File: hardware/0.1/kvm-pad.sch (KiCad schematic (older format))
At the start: 10 parts, among them J1 USB_C_Receptacle_USB2.0, J2 USB_C_Receptacle_USB2.0, U1 USBLC6-2SC6, U2 USBLC6-2SC6

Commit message: add mcu + 2x4 switches + icsp
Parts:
- added C1, C6: 1u, symbol Device:C
- added C2, C3: 100n, symbol Device:C
- added C4, C5: 22p, symbol Device:C
- added D1, D2, D3, D4, D5, D6, D7, D8: D, Diode_SMD:D_SOD-123, symbol Device:D_Small
- added J3: AVR-ISP-6, josh-connectors:AVR_PROG_2.54_SMT, symbol Connector:AVR-ISP-6
- added K1, K2, K3, K4, K5, K6, K7, K8: KEYSW, josh-keyboard:MX_KEYSWITCH, symbol Switch:SW_Push
- added R1, R2: 22R, symbol Device:R
- added R3: 10K, symbol Device:R
- added U2: ATMEGA32U4, symbol josh-ic:ATMEGA32U4
- added Y1: 16MHz, symbol Device:Crystal_GND24_Small
- renumbered U2 to U3
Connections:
- net GND: now also C1.2, C2.2, C3.2, C4.2, C5.2, C6.2, J3.6 (GND), R3.2, U2.15 (GND), U2.23 (GND), U2.35 (GND), U2.43 (GND), U2.5 (UGnd), Y1.2, Y1.4
- new net: C4.1, U2.16 (XTAL1), Y1.1
- new net: C5.1, U2.17 (XTAL2), Y1.3
- new net: R2.1, U2.3 (D-)
- new net: R3.1, U2.33 (PE2/~HWB)
- new net: R1.1, U2.4 (D+)
- new net: C6.1, U2.6 (UCap)
- new net: D1.2 (A), K1.2
- new net: D5.2 (A), K5.2
- new net: D2.2 (A), K2.2
- new net: D6.2 (A), K6.2
- new net: D4.2 (A), K4.2
- new net: D8.2 (A), K8.2
- new net: D7.2 (A), K7.2
- new net: D3.2 (A), K3.2
- new net +5V: C1.1, C2.1, C3.1, J3.2 (VCC), U2.14 (VCC), U2.2 (UVcc), U2.24 (AVCC), U2.34 (VCC), U2.42 (AREF), U2.44 (AVCC), U2.7 (VBus)
- new net MCU_D+: R1.2
- new net MCU_D-: R2.2
- new net MISO: J3.1 (MISO), U2.11 (PB3/MISO)
- new net MOSI: J3.4 (MOSI), U2.10 (PB2/MOSI)
- new net SCK: J3.3 (SCK), U2.9 (PB1/SCK)
- new net SWITCH: U2.27 (PD7)
- new net col1: K1.1, K5.1, U2.18 (PD0)
- new net col2: K2.1, K6.1, U2.19 (PD1)
- new net col3: K3.1, K7.1, U2.20 (PD2)
- new net col4: K4.1, K8.1, U2.21 (PD3)
- new net nRST: J3.5 (~RST), U2.13 (~RESET)
- new net row1: D1.1 (K), D2.1 (K), D3.1 (K), D4.1 (K), U2.41 (PF0)
- new net row2: D5.1 (K), D6.1 (K), D7.1 (K), D8.1 (K), U2.40 (PF1)
- no-connect marks 7 -> 19
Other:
- note added: "ICSP"
- note added: "Microcontroller"
- note added: "Switch Array"

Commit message: Update jkl & footprints
USBA / Kailh Choc / ATMEGA32U4-AU
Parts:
- K1, K2, K3, K4, K5, K6, K7, K8: footprint josh-keyboard:MX_KEYSWITCH -> josh-keyboard:Choc_Hotswap
- U2: footprint (none) -> josh-dfn-qfn:ATMEGA32U4-AU
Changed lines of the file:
@@
 F 0 "U2" H 5825 3962 60  0000 C CNN
 F 1 "ATMEGA32U4" H 5825 3856 60  0000 C CNN
-F 2 "" H 6025 2625 60  0000 C CNN
+F 2 "josh-dfn-qfn:ATMEGA32U4-AU" H 6025 2625 60  0001 C CNN
 F 3 "" H 6025 2625 60  0000 C CNN
 	1    6025 2625
@@
 F 0 "K1" H 7875 1425 60  0000 C CNN
 F 1 "KEYSW" H 7875 1150 60  0001 C CNN
-F 2 "josh-keyboard:MX_KEYSWITCH" H 7875 1250 60  0001 C CNN
+F 2 "josh-keyboard:Choc_Hotswap" H 7875 1250 60  0001 C CNN
 F 3 "" H 7875 1250 60  0000 C CNN
 F 4 "" H 7875 1250 50  0001 C CNN "Notes"
@@
 F 0 "K5" H 7875 2025 60  0000 C CNN
 F 1 "KEYSW" H 7875 1750 60  0001 C CNN
-F 2 "josh-keyboard:MX_KEYSWITCH" H 7875 1850 60  0001 C CNN
+F 2 "josh-keyboard:Choc_Hotswap" H 7875 1850 60  0001 C CNN
 F 3 "" H 7875 1850 60  0000 C CNN
 F 4 "" H 7875 1850 50  0001 C CNN "Notes"
@@
 F 0 "K2" H 8775 1425 60  0000 C CNN
 F 1 "KEYSW" H 8775 1150 60  0001 C CNN
-F 2 "josh-keyboard:MX_KEYSWITCH" H 8775 1250 60  0001 C CNN
+F 2 "josh-keyboard:Choc_Hotswap" H 8775 1250 60  0001 C CNN
 F 3 "" H 8775 1250 60  0000 C CNN
 F 4 "" H 8775 1250 50  0001 C CNN "Notes"
@@
 F 0 "K6" H 8775 2025 60  0000 C CNN
 F 1 "KEYSW" H 8775 1750 60  0001 C CNN
-F 2 "josh-keyboard:MX_KEYSWITCH" H 8775 1850 60  0001 C CNN
+F 2 "josh-keyboard:Choc_Hotswap" H 8775 1850 60  0001 C CNN
 F 3 "" H 8775 1850 60  0000 C CNN
 F 4 "" H 8775 1850 50  0001 C CNN "Notes"
@@
 F 0 "K4" H 10575 1425 60  0000 C CNN
 F 1 "KEYSW" H 10575 1150 60  0001 C CNN
-F 2 "josh-keyboard:MX_KEYSWITCH" H 10575 1250 60  0001 C CNN
+F 2 "josh-keyboard:Choc_Hotswap" H 10575 1250 60  0001 C CNN
 F 3 "" H 10575 1250 60  0000 C CNN
 F 4 "" H 10575 1250 50  0001 C CNN "Notes"
@@
 F 0 "K8" H 10575 2025 60  0000 C CNN
 F 1 "KEYSW" H 10575 1750 60  0001 C CNN
-F 2 "josh-keyboard:MX_KEYSWITCH" H 10575 1850 60  0001 C CNN
+F 2 "josh-keyboard:Choc_Hotswap" H 10575 1850 60  0001 C CNN
 F 3 "" H 10575 1850 60  0000 C CNN
 F 4 "" H 10575 1850 50  0001 C CNN "Notes"
@@
 F 0 "K7" H 9675 2025 60  0000 C CNN
 F 1 "KEYSW" H 9675 1750 60  0001 C CNN
-F 2 "josh-keyboard:MX_KEYSWITCH" H 9675 1850 60  0001 C CNN
+F 2 "josh-keyboard:Choc_Hotswap" H 9675 1850 60  0001 C CNN
 F 3 "" H 9675 1850 60  0000 C CNN
 F 4 "" H 9675 1850 50  0001 C CNN "Notes"
@@
 F 0 "K3" H 9700 1425 60  0000 C CNN
 F 1 "KEYSW" H 9700 1150 60  0001 C CNN
-F 2 "josh-keyboard:MX_KEYSWITCH" H 9700 1250 60  0001 C CNN
+F 2 "josh-keyboard:Choc_Hotswap" H 9700 1250 60  0001 C CNN
 F 3 "" H 9700 1250 60  0000 C CNN
 F 4 "" H 9700 1250 50  0001 C CNN "Notes"

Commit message: Add missing footprints
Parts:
- C1, C2, C3, C4, C5, C6: footprint (none) -> Capacitor_SMD:C_0603_1608Metric
- R1, R2, R3: footprint (none) -> Resistor_SMD:R_0603_1608Metric
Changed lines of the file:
@@
 F 0 "C3" V 4625 1250 50  0000 C CNN
 F 1 "100n" V 4725 1250 50  0000 C CNN
-F 2 "" H 4713 1250 50  0001 C CNN
+F 2 "Capacitor_SMD:C_0603_1608Metric" H 4713 1250 50  0001 C CNN
 F 3 "~" H 4675 1400 50  0001 C CNN
 	1    4675 1400
@@
 F 0 "C2" V 4625 1025 50  0000 C CNN
 F 1 "100n" V 4725 1025 50  0000 C CNN
-F 2 "" H 4713 1025 50  0001 C CNN
+F 2 "Capacitor_SMD:C_0603_1608Metric" H 4713 1025 50  0001 C CNN
 F 3 "~" H 4675 1175 50  0001 C CNN
 	1    4675 1175
@@
 F 0 "C1" V 4625 800 50  0000 C CNN
 F 1 "1u" V 4725 800 50  0000 C CNN
-F 2 "" H 4713 800 50  0001 C CNN
+F 2 "Capacitor_SMD:C_0603_1608Metric" H 4713 800 50  0001 C CNN
 F 3 "~" H 4675 950 50  0001 C CNN
 	1    4675 950
@@
 F 0 "C4" V 4325 2775 50  0000 C CNN
 F 1 "22p" V 4425 2775 50  0000 C CNN
-F 2 "" H 4413 2775 50  0001 C CNN
+F 2 "Capacitor_SMD:C_0603_1608Metric" H 4413 2775 50  0001 C CNN
 F 3 "~" H 4375 2925 50  0001 C CNN
 	1    4375 2925
@@
 F 0 "C5" V 4325 2975 50  0000 C CNN
 F 1 "22p" V 4425 2975 50  0000 C CNN
-F 2 "" H 4413 2975 50  0001 C CNN
+F 2 "Capacitor_SMD:C_0603_1608Metric" H 4413 2975 50  0001 C CNN
 F 3 "~" H 4375 3125 50  0001 C CNN
 	1    4375 3125
@@
 F 0 "R3" H 4695 3721 50  0000 L CNN
 F 1 "10K" H 4695 3630 50  0000 L CNN
-F 2 "" V 4555 3675 50  0001 C CNN
+F 2 "Resistor_SMD:R_0603_1608Metric" V 4555 3675 50  0001 C CNN
 F 3 "~" H 4625 3675 50  0001 C CNN
 	1    4625 3675
@@
 F 0 "C6" H 4440 3721 50  0000 L CNN
 F 1 "1u" H 4440 3630 50  0000 L CNN
-F 2 "" H 4363 3525 50  0001 C CNN
+F 2 "Capacitor_SMD:C_0603_1608Metric" H 4363 3525 50  0001 C CNN
 F 3 "~" H 4325 3675 50  0001 C CNN
 	1    4325 3675
@@
 F 0 "R1" V 4725 2375 50  0000 C CNN
 F 1 "22R" V 4825 2375 50  0000 C CNN
-F 2 "" V 4755 2375 50  0001 C CNN
+F 2 "Resistor_SMD:R_0603_1608Metric" V 4755 2375 50  0001 C CNN
 F 3 "~" H 4825 2375 50  0001 C CNN
 	1    4825 2375
@@
 F 0 "R2" V 4925 2475 50  0000 C CNN
 F 1 "22R" V 4825 2475 50  0000 C CNN
-F 2 "" V 4755 2475 50  0001 C CNN
+F 2 "Resistor_SMD:R_0603_1608Metric" V 4755 2475 50  0001 C CNN
 F 3 "~" H 4825 2475 50  0001 C CNN
 	1    4825 2475

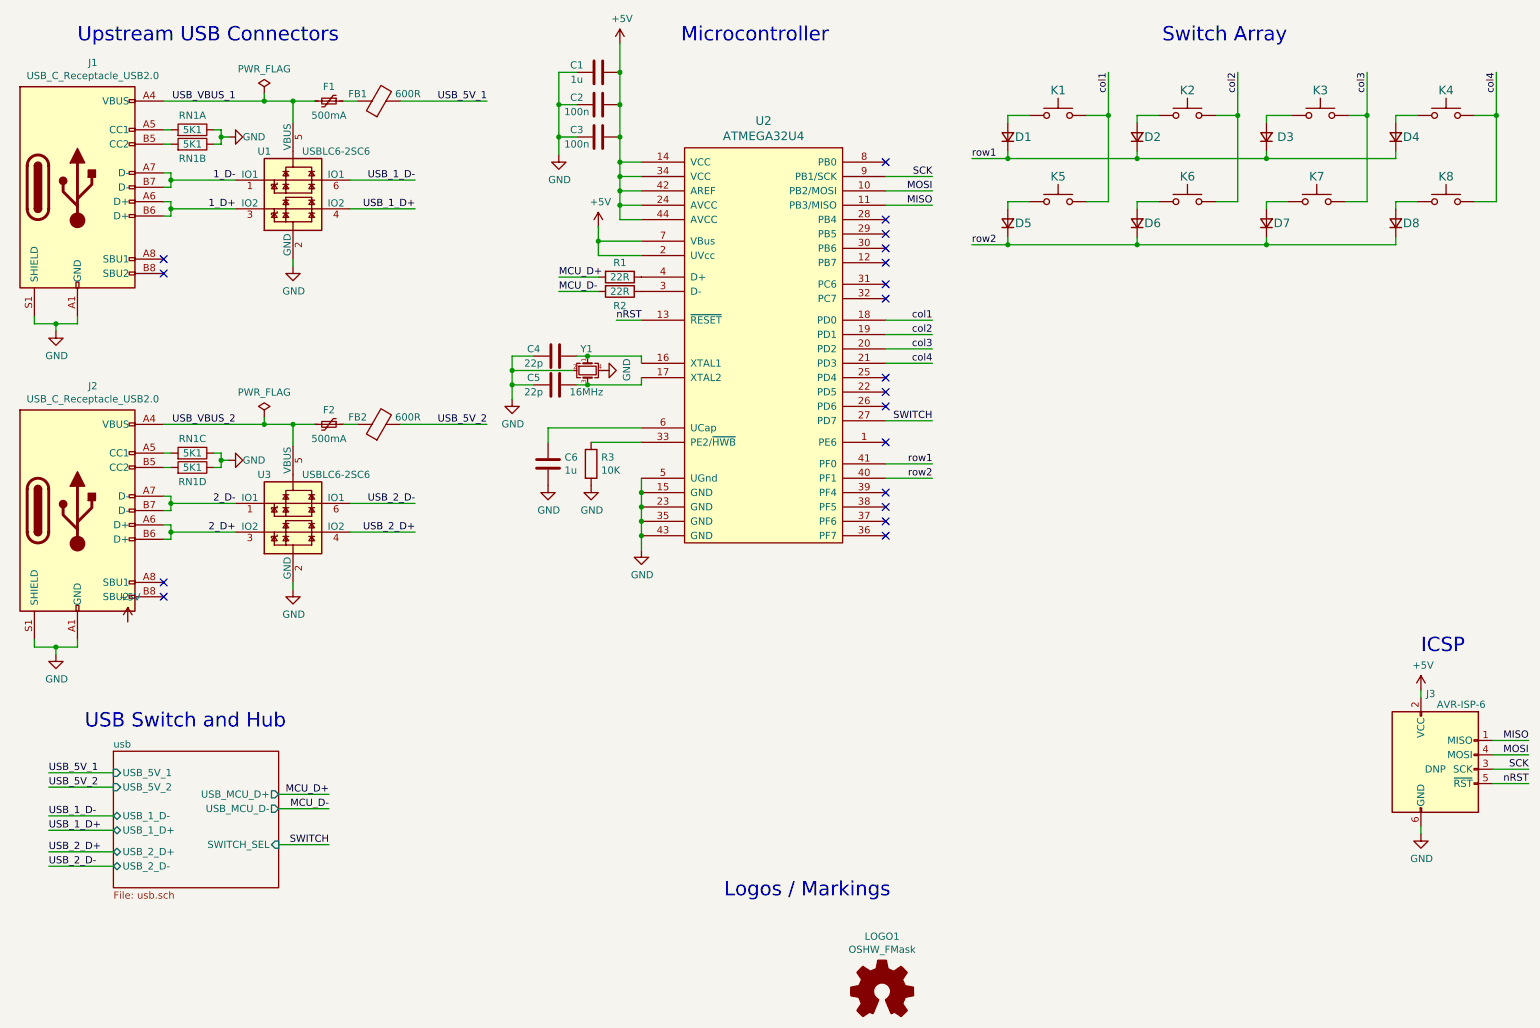
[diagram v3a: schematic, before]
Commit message: Add RGB LEDs
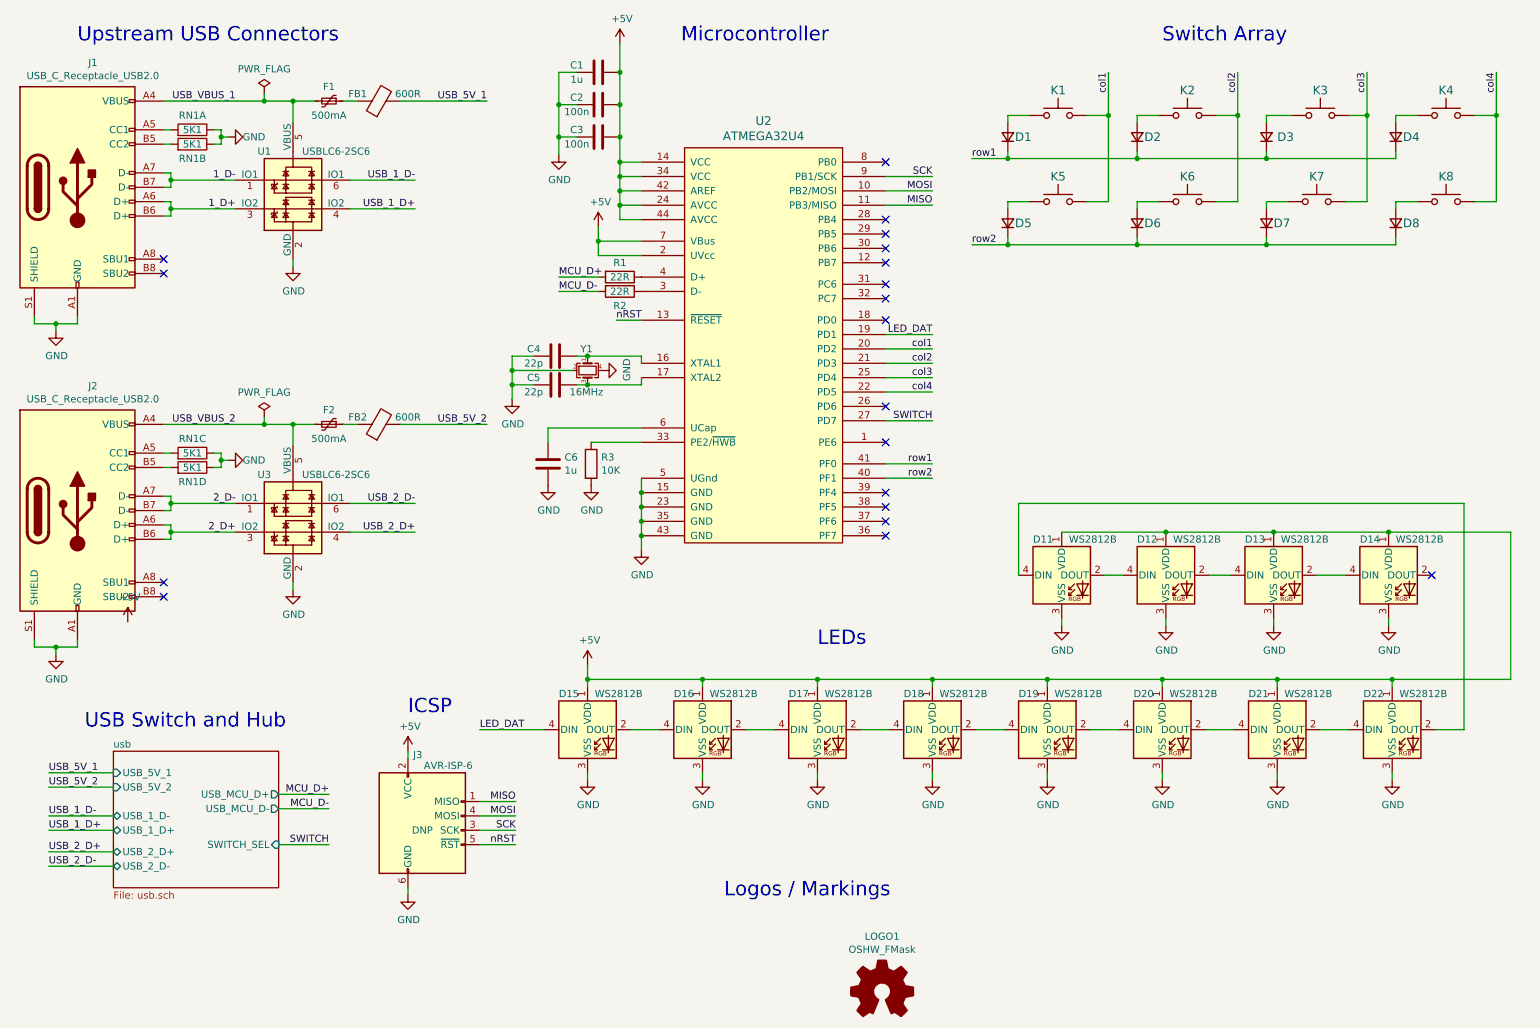
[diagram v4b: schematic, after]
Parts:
- added D11, D12, D13, D14, D15, D16, D17, D18, D19, D20, D21, D22: WS2812B, josh-led:SK8612-MINI-E, symbol LED:WS2812B
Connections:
- net +5V: now also D11.1 (VDD), D12.1 (VDD), D13.1 (VDD), D14.1 (VDD), D15.1 (VDD), D16.1 (VDD), D17.1 (VDD), D18.1 (VDD), D19.1 (VDD), D20.1 (VDD), D21.1 (VDD), D22.1 (VDD)
- net GND: now also D11.3 (VSS), D12.3 (VSS), D13.3 (VSS), D14.3 (VSS), D15.3 (VSS), D16.3 (VSS), D17.3 (VSS), D18.3 (VSS), D19.3 (VSS), D20.3 (VSS), D21.3 (VSS), D22.3 (VSS)
- net col1: now also U2.20 (PD2); no longer U2.18 (PD0)
- net col2: now also U2.21 (PD3); no longer U2.19 (PD1)
- net col3: now also U2.25 (PD4); no longer U2.20 (PD2)
- net col4: now also U2.22 (PD5); no longer U2.21 (PD3)
- new net: D15.2 (DOUT), D16.4 (DIN)
- new net: D16.2 (DOUT), D17.4 (DIN)
- new net: D17.2 (DOUT), D18.4 (DIN)
- new net: D18.2 (DOUT), D19.4 (DIN)
- new net: D19.2 (DOUT), D20.4 (DIN)
- new net: D20.2 (DOUT), D21.4 (DIN)
- new net: D21.2 (DOUT), D22.4 (DIN)
- new net: D11.4 (DIN), D22.2 (DOUT)
- new net: D12.2 (DOUT), D13.4 (DIN)
- new net: D11.2 (DOUT), D12.4 (DIN)
- new net: D13.2 (DOUT), D14.4 (DIN)
- new net LED_DAT: D15.4 (DIN), U2.19 (PD1)
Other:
- note added: "LEDs"
- moved on the sheet: J3

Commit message: Update jkl, adjust schema accordingly, 32u4+16MHz
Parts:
- U2: footprint josh-dfn-qfn:ATMEGA32U4-AU -> Package_QFP:TQFP-44_10x10mm_P0.8mm
- Y1: footprint (none) -> josh-oscillators:Crystal_SMD_3225-4Pin_3.2x2.5mm
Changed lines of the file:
@@
 F 0 "Y1" V 4450 2975 50  0000 L CNN
 F 1 "16MHz" V 4750 2900 50  0000 L CNN
-F 2 "" H 4600 3025 50  0001 C CNN
+F 2 "josh-oscillators:Crystal_SMD_3225-4Pin_3.2x2.5mm" H 4600 3025 50  0001 C CNN
 F 3 "~" H 4600 3025 50  0001 C CNN
 	1    4600 3025
@@
 F 0 "U2" H 5825 3962 60  0000 C CNN
 F 1 "ATMEGA32U4" H 5825 3856 60  0000 C CNN
-F 2 "josh-dfn-qfn:ATMEGA32U4-AU" H 6025 2625 60  0001 C CNN
+F 2 "Package_QFP:TQFP-44_10x10mm_P0.8mm" H 6025 2625 60  0001 C CNN
 F 3 "" H 6025 2625 60  0000 C CNN
 	1    6025 2625

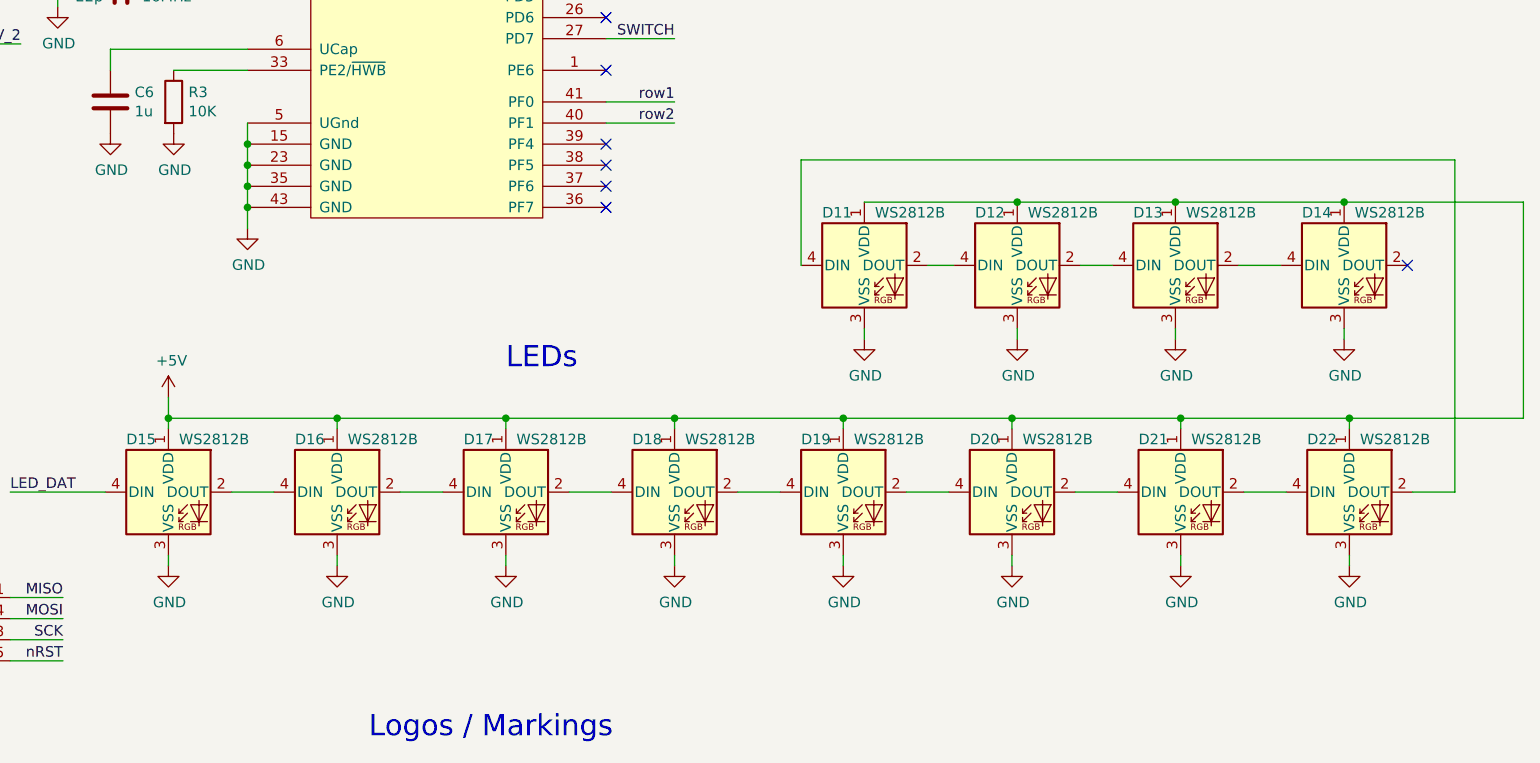
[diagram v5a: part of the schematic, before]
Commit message: Clean up WS2812 routing
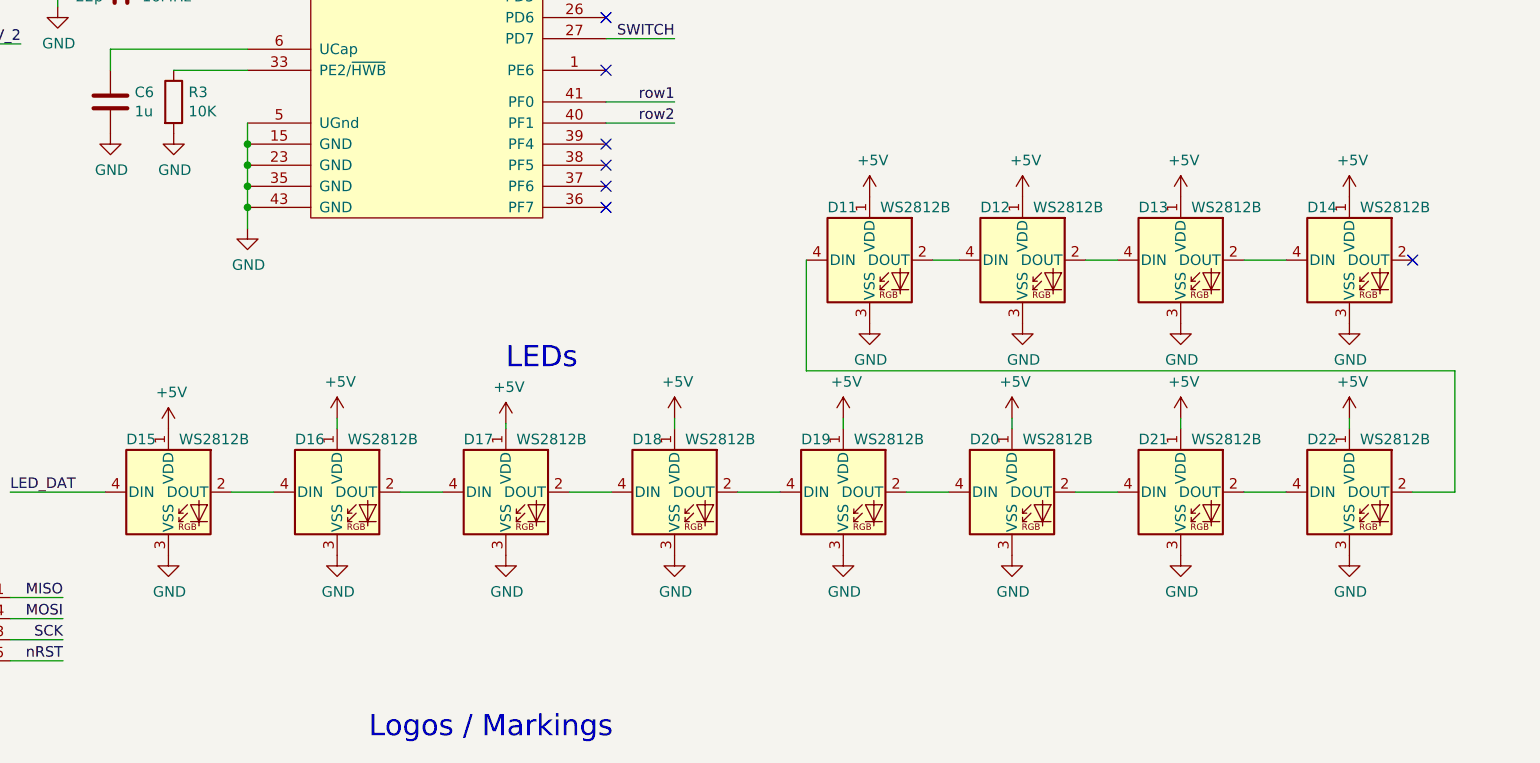
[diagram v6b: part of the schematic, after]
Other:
- moved on the sheet: D11, D12, D13, D14
